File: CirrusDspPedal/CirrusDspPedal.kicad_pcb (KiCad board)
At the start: 2 copper layers, 112.5 x 86.4 mm, 94 parts, among them J1 MonoJack2Switch, J2 MonoJack2Switch, J3 Conn_02x05_Odd_Even, J4 Barrel_Jack_Switch, J5 MonoJack2Switch, J6 Micro_SD_Card_Det, J7 Conn_01x01, K1 HFD4/3_S, Q1 DMG2302U, SW1 P26L-1D-RND MTL, SW2 P26L-1D-RND MTL, SW3 SW_SPST, SW4 SW_SPST, U1 CS5343, U2 74AHC1G126, U3 CS4344, U4 SE8250X2_SOT23, U5 MCP1703A-1202_SOT223, U6 MCP601-xOT, U7 STM32F405RGTx

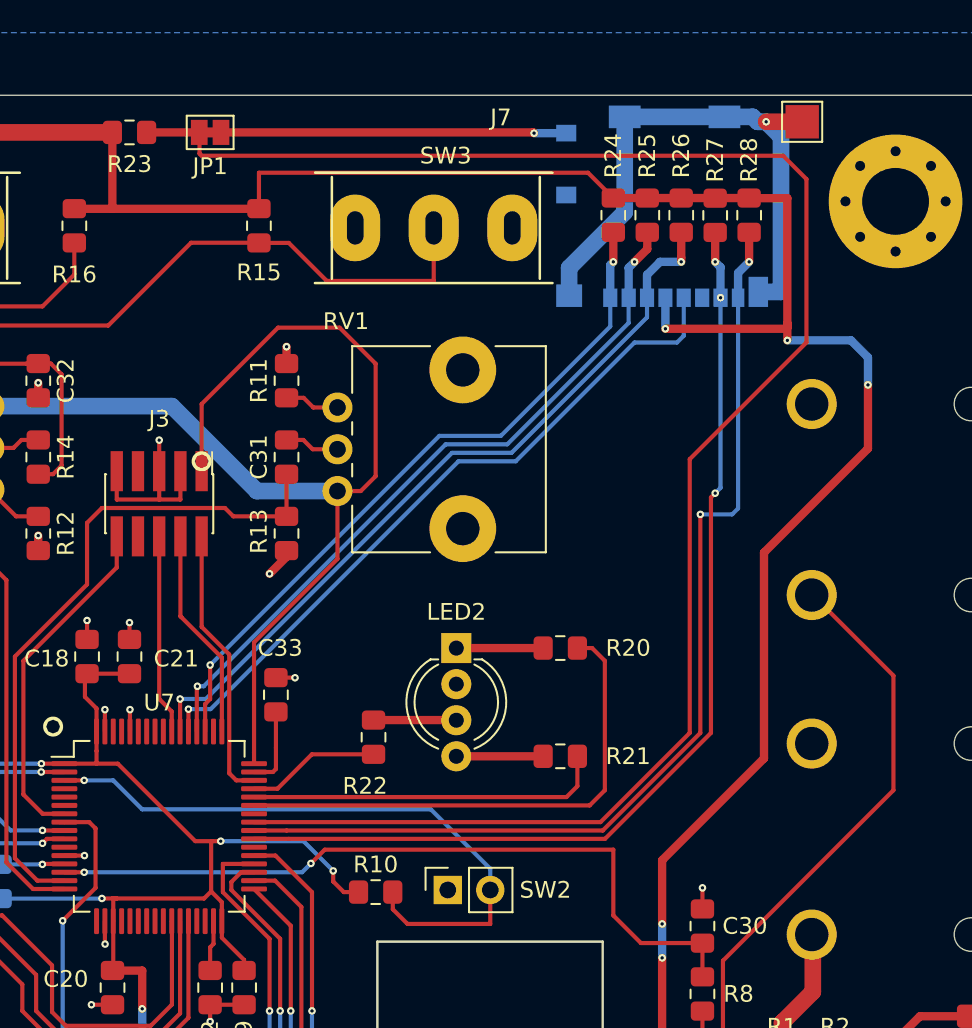
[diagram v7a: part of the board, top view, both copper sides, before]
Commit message: replaced SDIO connector
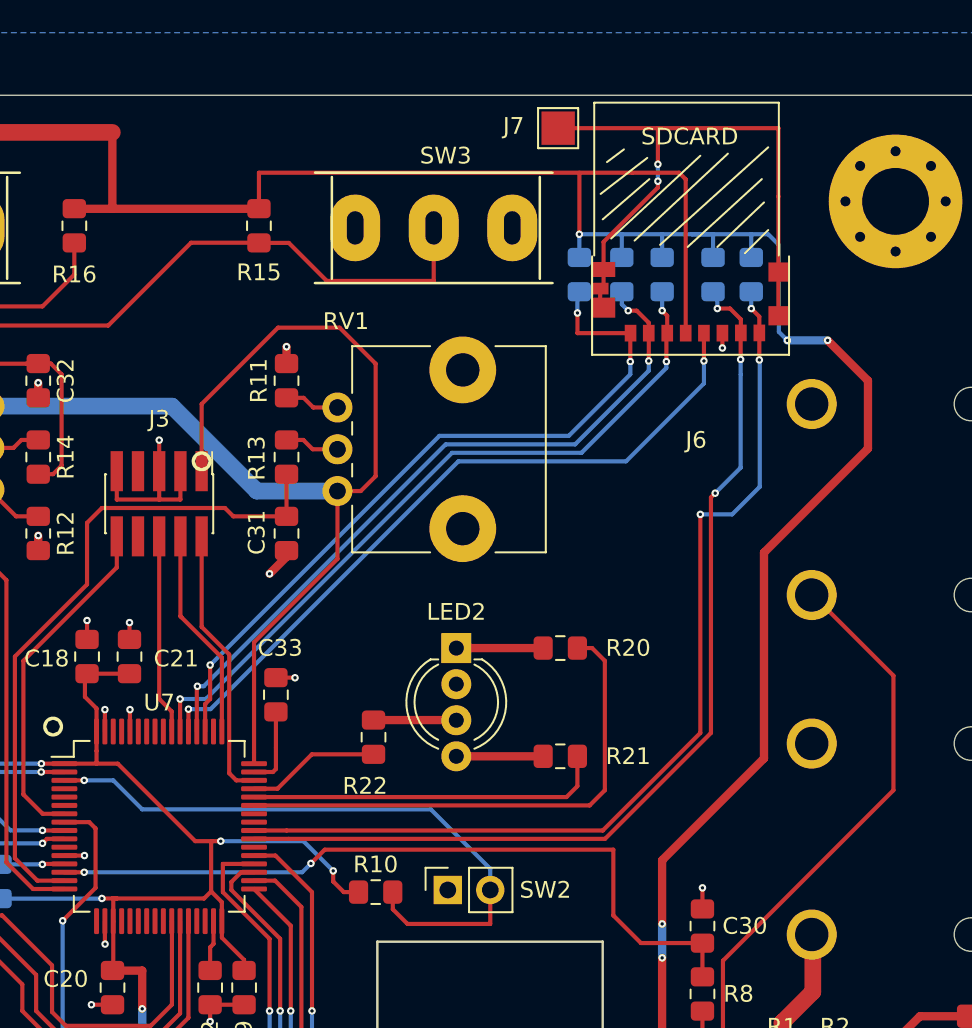
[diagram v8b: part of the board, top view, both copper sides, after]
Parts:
- removed JP1: Jumper_NC_Small, Jumper:SolderJumper-2_P1.3mm_Bridged_Pad1.0x1.5mm
- removed R23: 10K, Resistor_SMD:R_0805_2012Metric_Pad1.15x1.40mm_HandSolder
- C30, C31, C32: value 180pF C0G -> 100nF
- J6: value Micro_SD_Card_Det -> Micro_SD_Card; footprint Connector_Card:microSD_HC_Molex_104031-0811 -> Molex_SDIO:Molex_SDIO_475710001; moved to F.Cu
- R24, R25, R26, R27, R28: moved to B.Cu
- moved J7 14.6 mm to (172.2, 56.5)
- moved R24 4.10 mm to (173.5, 65.3)
- moved R25 3.87 mm to (176.0, 65.3)
- moved R26 3.74 mm to (178.4, 65.3)
- moved R28 3.56 mm to (183.8, 65.3)
- moved R27 3.55 mm to (181.5, 65.3)
- moved J6 3.19 mm to (179.7, 64.1), turned to 180 degrees
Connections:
- J6 pad 9: GND -> GNDPWR
- U7 pad 41: /MicroSD/uSD_Detect -> Net-(U7-Pad41)
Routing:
- net /MicroSD/uSD_Detect: track 105.7 -> 0.00 mm
- net Net-(J6-Pad10): track 20.7 -> 0.00 mm, vias 1 -> 0
- net +3V3: track 405.4 -> 419.2 mm
- net /MicroSD/uSD_D1: track 61.5 -> 58.3 mm, vias 2 -> 3
- net GNDPWR: track 34.7 -> 37.2 mm, vias 1 -> 2
- net /MicroSD/uSD_D2: track 42.2 -> 44.6 mm, vias 2 -> 3
- net /MicroSD/uSD_D0: track 60.3 -> 58.2 mm
- net /MicroSD/uSD_CMD: track 46.0 -> 44.1 mm, vias 2 -> 3
- net GND: track 111.0 -> 111.9 mm, vias 57 -> 58
- net /MicroSD/uSD_CLK: track 42.5 -> 43.3 mm, vias 1 -> 2
- net /MicroSD/uSD_D3: track 43.4 -> 43.1 mm, vias 2 -> 3
